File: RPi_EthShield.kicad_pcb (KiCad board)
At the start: 2 copper layers, 65 x 30.5 mm, 22 parts, among them IC1 DS1233AZ-10+, J1 HR911105A, J2 RPi_GPIO, U1 ENC28J60x-SO, U2 LM1117-3.3, Y1 Crystal

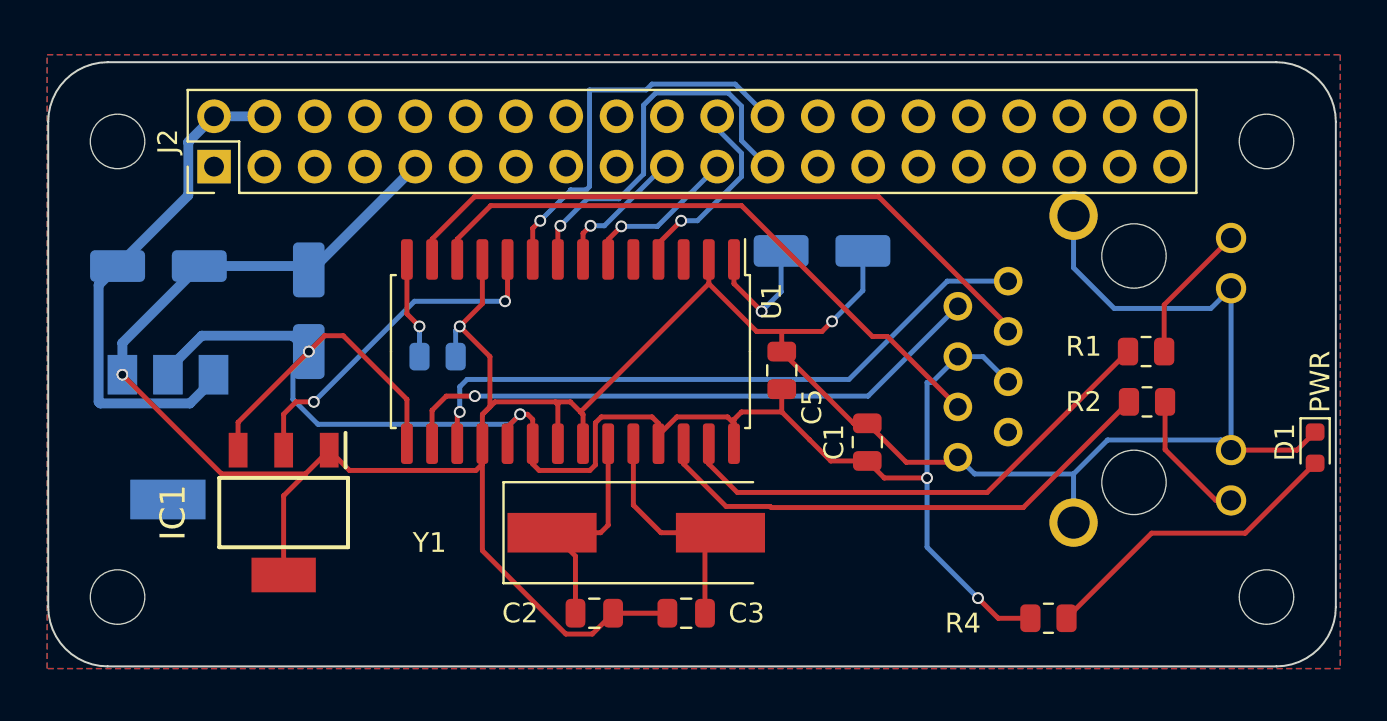
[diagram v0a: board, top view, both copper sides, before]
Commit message: footprint for DS1233a fixed
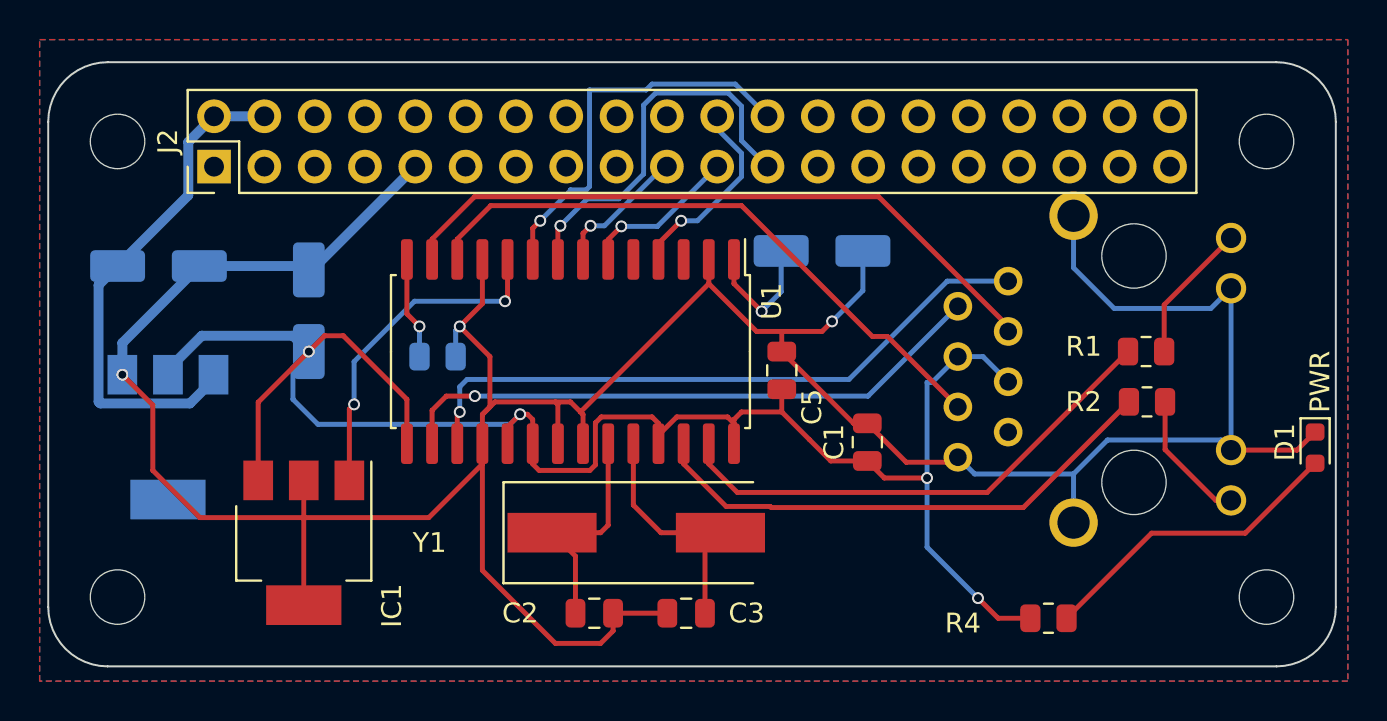
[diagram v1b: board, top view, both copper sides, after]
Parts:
- IC1: footprint symbols:SOT230P700X180-4N -> EthShield:DS1233_SOT223
- Y1: value Crystal -> 25MHz
- moved IC1 1.83 mm to (25.4, 48.3)
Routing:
- net GND: track 162.8 -> 167.9 mm
- net +3V3: track 93.0 -> 94.1 mm
